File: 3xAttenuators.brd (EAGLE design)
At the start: 19 x 109.5 mm, 9 parts

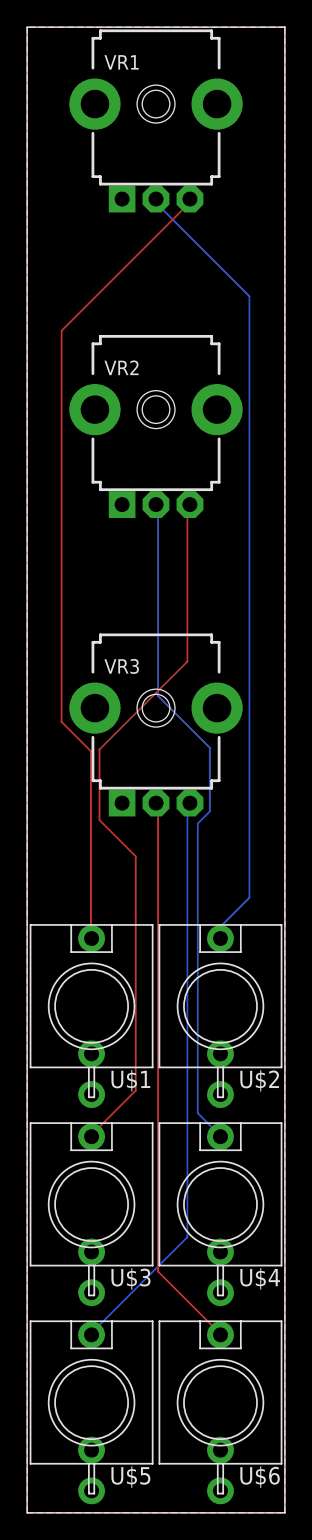
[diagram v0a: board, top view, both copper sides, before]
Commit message: adding rendered images of pcbs
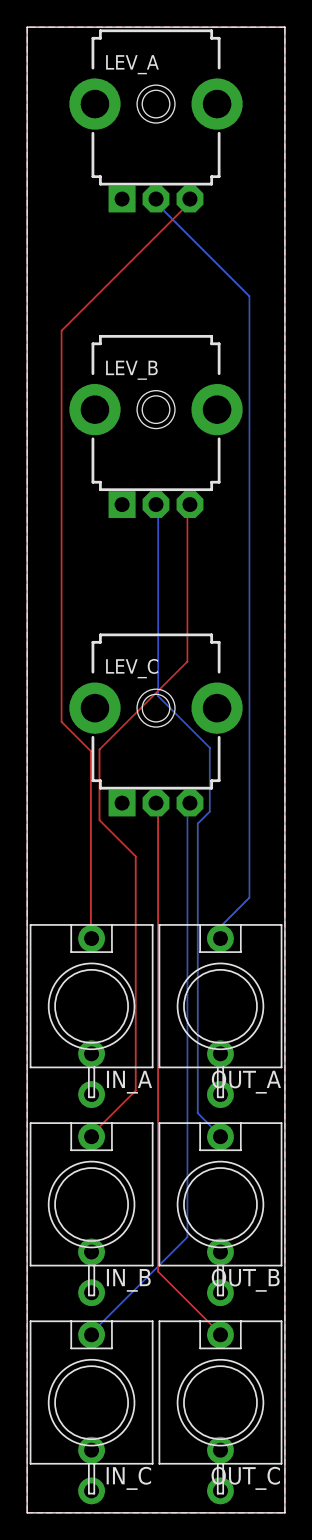
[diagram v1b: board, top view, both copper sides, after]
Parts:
- renumbered U$1 to IN_A, U$2 to OUT_A, U$3 to IN_B, U$4 to OUT_B, U$5 to IN_C, U$6 to OUT_C, VR1 to LEV_A, VR2 to LEV_B, VR3 to LEV_C
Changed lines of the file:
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@@
 </layers>
 <board>
+<fusionsync huburn="a.YnVzaW5lc3M6bXl1dzIwNDI" projecturn="a.YnVzaW5lc3M6bXl1dzIwNDIjRDIwMjIwNzA2NTM3OTQ1NzI2" f3durn="urn:adsk.wipprod:dm.lineage:7zFyWXWUTs2JKTcB2DoE3w" pcbguid="0d0611a9-9bd2-43dd-86c0-04be61c52497" lastpulledtime="" lastsyncedchangeguid="" latestrevisionid="42cfb351-0af1-4083-9baa-e86a03af3349" lastsyncedrevisionid="42cfb351-0af1-4083-9baa-e86a03af3349" lastboardhashguid="bff14a14-c0db-dd21-dd38-d28ebede1a6b" lastpushedtime="2022-12-21T20:23:48Z" linktopcb3d="true"/>
 <plain>
 <wire x1="0" y1="0" x2="19" y2="0" width="0" layer="20"/>
@@
 </autorouter>
 <elements>
-<element name="U$1" library="ES-2144 LPF Module" library_urn="urn:adsk.eagle:library:35649419" package="THONKICONN_WQP-PJ301M-12_JACK" package3d_urn="urn:adsk.eagle:package:35649430/2" value="THONKICONN_WQP-PJ301M-12_JACK" x="4.75" y="37.33" smashed="yes">
+<element name="IN_A" library="ES-2144 LPF Module" library_urn="urn:adsk.eagle:library:35649419" package="THONKICONN_WQP-PJ301M-12_JACK" package3d_urn="urn:adsk.eagle:package:35649430/2" value="THONKICONN_WQP-PJ301M-12_JACK" x="4.75" y="37.33" smashed="yes">
 <attribute name="NAME" x="9.2204" y="32.5802" size="1.27" layer="21" rot="R180"/>
 </element>
-<element name="U$2" library="ES-2144 LPF Module" library_urn="urn:adsk.eagle:library:35649419" package="THONKICONN_WQP-PJ301M-12_JACK" package3d_urn="urn:adsk.eagle:package:35649430/2" value="THONKICONN_WQP-PJ301M-12_JACK" x="14.25" y="37.33" smashed="yes">
+<element name="OUT_A" library="ES-2144 LPF Module" library_urn="urn:adsk.eagle:library:35649419" package="THONKICONN_WQP-PJ301M-12_JACK" package3d_urn="urn:adsk.eagle:package:35649430/2" value="THONKICONN_WQP-PJ301M-12_JACK" x="14.25" y="37.33" smashed="yes">
 <attribute name="NAME" x="18.7204" y="32.5802" size="1.27" layer="21" rot="R180"/>
 </element>
-<element name="U$3" library="ES-2144 LPF Module" library_urn="urn:adsk.eagle:library:35649419" package="THONKICONN_WQP-PJ301M-12_JACK" package3d_urn="urn:adsk.eagle:package:35649430/2" value="THONKICONN_WQP-PJ301M-12_JACK" x="4.75" y="22.725" smashed="yes">
+<element name="IN_B" library="ES-2144 LPF Module" library_urn="urn:adsk.eagle:library:35649419" package="THONKICONN_WQP-PJ301M-12_JACK" package3d_urn="urn:adsk.eagle:package:35649430/2" value="THONKICONN_WQP-PJ301M-12_JACK" x="4.75" y="22.725" smashed="yes">
 <attribute name="NAME" x="9.2204" y="17.9752" size="1.27" layer="21" rot="R180"/>
 </element>
-<element name="U$4" library="ES-2144 LPF Module" library_urn="urn:adsk.eagle:library:35649419" package="THONKICONN_WQP-PJ301M-12_JACK" package3d_urn="urn:adsk.eagle:package:35649430/2" value="THONKICONN_WQP-PJ301M-12_JACK" x="14.25" y="22.725" smashed="yes">
+<element name="OUT_B" library="ES-2144 LPF Module" library_urn="urn:adsk.eagle:library:35649419" package="THONKICONN_WQP-PJ301M-12_JACK" package3d_urn="urn:adsk.eagle:package:35649430/2" value="THONKICONN_WQP-PJ301M-12_JACK" x="14.25" y="22.725" smashed="yes">
 <attribute name="NAME" x="18.7204" y="17.9752" size="1.27" layer="21" rot="R180"/>
 </element>
-<element name="VR1" library="ES-2144 LPF Module" library_urn="urn:adsk.eagle:library:35649419" package="MUSICTHINGMODULAR_9MM_SNAP-IN_POT" package3d_urn="urn:adsk.eagle:package:35649433/2" value="B50K" x="9.5" y="103.83" smashed="yes">
+<element name="LEV_A" library="ES-2144 LPF Module" library_urn="urn:adsk.eagle:library:35649419" package="MUSICTHINGMODULAR_9MM_SNAP-IN_POT" package3d_urn="urn:adsk.eagle:package:35649433/2" value="B50K" x="9.5" y="103.83" smashed="yes">
 <attribute name="NAME" x="5.69" y="106.37" size="1.0668" layer="25"/>
 <attribute name="VALUE" x="5.69" y="100.02" size="1.27" layer="27"/>
 </element>
-<element name="VR2" library="ES-2144 LPF Module" library_urn="urn:adsk.eagle:library:35649419" package="MUSICTHINGMODULAR_9MM_SNAP-IN_POT" package3d_urn="urn:adsk.eagle:package:35649433/2" value="B50K" x="9.5" y="81.31" smashed="yes">
+<element name="LEV_B" library="ES-2144 LPF Module" library_urn="urn:adsk.eagle:library:35649419" package="MUSICTHINGMODULAR_9MM_SNAP-IN_POT" package3d_urn="urn:adsk.eagle:package:35649433/2" value="B50K" x="9.5" y="81.31" smashed="yes">
 <attribute name="NAME" x="5.69" y="83.85" size="1.0668" layer="25"/>
 <attribute name="VALUE" x="5.69" y="77.5" size="1.27" layer="27"/>
 </element>
-<element name="U$5" library="ES-2144 LPF Module" library_urn="urn:adsk.eagle:library:35649419" package="THONKICONN_WQP-PJ301M-12_JACK" package3d_urn="urn:adsk.eagle:package:35649430/2" value="THONKICONN_WQP-PJ301M-12_JACK" x="4.75" y="8.12" smashed="yes">
+<element name="IN_C" library="ES-2144 LPF Module" library_urn="urn:adsk.eagle:library:35649419" package="THONKICONN_WQP-PJ301M-12_JACK" package3d_urn="urn:adsk.eagle:package:35649430/2" value="THONKICONN_WQP-PJ301M-12_JACK" x="4.75" y="8.12" smashed="yes">
 <attribute name="NAME" x="9.2204" y="3.3702" size="1.27" layer="21" rot="R180"/>
 </element>
-<element name="U$6" library="ES-2144 LPF Module" library_urn="urn:adsk.eagle:library:35649419" package="THONKICONN_WQP-PJ301M-12_JACK" package3d_urn="urn:adsk.eagle:package:35649430/2" value="THONKICONN_WQP-PJ301M-12_JACK" x="14.25" y="8.12" smashed="yes">
+<element name="OUT_C" library="ES-2144 LPF Module" library_urn="urn:adsk.eagle:library:35649419" package="THONKICONN_WQP-PJ301M-12_JACK" package3d_urn="urn:adsk.eagle:package:35649430/2" value="THONKICONN_WQP-PJ301M-12_JACK" x="14.25" y="8.12" smashed="yes">
 <attribute name="NAME" x="18.7204" y="3.3702" size="1.27" layer="21" rot="R180"/>
 </element>
-<element name="VR3" library="ES-2144 LPF Module" library_urn="urn:adsk.eagle:library:35649419" package="MUSICTHINGMODULAR_9MM_SNAP-IN_POT" package3d_urn="urn:adsk.eagle:package:35649433/2" value="B50K" x="9.5" y="59.31" smashed="yes">
+<element name="LEV_C" library="ES-2144 LPF Module" library_urn="urn:adsk.eagle:library:35649419" package="MUSICTHINGMODULAR_9MM_SNAP-IN_POT" package3d_urn="urn:adsk.eagle:package:35649433/2" value="B50K" x="9.5" y="59.31" smashed="yes">
 <attribute name="NAME" x="5.69" y="61.85" size="1.0668" layer="25"/>
 <attribute name="VALUE" x="5.69" y="55.5" size="1.27" layer="27"/>
@@
 <signals>
 <signal name="N$3">
-<contactref element="U$3" pad="P$1"/>
-<contactref element="VR2" pad="3"/>
+<contactref element="IN_B" pad="P$1"/>
+<contactref element="LEV_B" pad="3"/>
 <wire x1="5.334" y1="28.321" x2="4.826" y2="27.813" width="0.127" layer="1"/>
 <wire x1="5.334" y1="28.448" x2="5.334" y2="28.321" width="0.127" layer="1"/>
@@
 </signal>
 <signal name="N$4">
-<contactref element="VR2" pad="2"/>
-<contactref element="U$4" pad="P$1"/>
+<contactref element="LEV_B" pad="2"/>
+<contactref element="OUT_B" pad="P$1"/>
 <wire x1="12.573" y1="29.464" x2="14.224" y2="27.813" width="0.127" layer="16"/>
 <wire x1="12.573" y1="50.8" x2="12.573" y2="29.464" width="0.127" layer="16"/>
@@
 </signal>
 <signal name="N$2">
-<contactref element="U$2" pad="P$1"/>
-<contactref element="VR1" pad="2"/>
+<contactref element="OUT_A" pad="P$1"/>
+<contactref element="LEV_A" pad="2"/>
 <wire x1="14.351" y1="43.307" x2="14.351" y2="42.418" width="0.127" layer="16"/>
 <wire x1="16.383" y1="45.339" x2="14.351" y2="43.307" width="0.127" layer="16"/>
@@
 </signal>
 <signal name="N$5">
-<contactref element="U$1" pad="P$1"/>
-<contactref element="VR1" pad="3"/>
+<contactref element="IN_A" pad="P$1"/>
+<contactref element="LEV_A" pad="3"/>
 <wire x1="4.699" y1="56.134" x2="4.699" y2="42.418" width="0.127" layer="1"/>
 <wire x1="2.54" y1="58.293" x2="4.699" y2="56.134" width="0.127" layer="1"/>
@@
 </signal>
 <signal name="N$1">
-<contactref element="U$5" pad="P$1"/>
-<contactref element="VR3" pad="3"/>
+<contactref element="IN_C" pad="P$1"/>
+<contactref element="LEV_C" pad="3"/>
 <wire x1="5.334" y1="13.716" x2="4.826" y2="13.208" width="0.127" layer="16"/>
 <wire x1="5.334" y1="13.843" x2="5.334" y2="13.716" width="0.127" layer="16"/>
@@
 </signal>
 <signal name="N$6">
-<contactref element="VR3" pad="2"/>
-<contactref element="U$6" pad="P$1"/>
+<contactref element="LEV_C" pad="2"/>
+<contactref element="OUT_C" pad="P$1"/>
 <wire x1="9.652" y1="17.78" x2="14.224" y2="13.208" width="0.127" layer="1"/>
 <wire x1="9.652" y1="52.07" x2="9.652" y2="17.78" width="0.127" layer="1"/>
@@
 <vertex x="19" y="0"/>
 </polygon>
-<contactref element="U$3" pad="P$3"/>
-<contactref element="VR2" pad="1"/>
-<contactref element="U$4" pad="P$3"/>
-<contactref element="U$1" pad="P$3"/>
-<contactref element="VR1" pad="1"/>
-<contactref element="U$2" pad="P$3"/>
-<contactref element="U$5" pad="P$3"/>
-<contactref element="VR3" pad="1"/>
-<contactref element="U$6" pad="P$3"/>
+<contactref element="IN_B" pad="P$3"/>
+<contactref element="LEV_B" pad="1"/>
+<contactref element="OUT_B" pad="P$3"/>
+<contactref element="IN_A" pad="P$3"/>
+<contactref element="LEV_A" pad="1"/>
+<contactref element="OUT_A" pad="P$3"/>
+<contactref element="IN_C" pad="P$3"/>
+<contactref element="LEV_C" pad="1"/>
+<contactref element="OUT_C" pad="P$3"/>
 <polygon width="0.1524" layer="16">
 <vertex x="19" y="109.5"/>
@@
 </note>
 <note version="8.3" severity="warning">
+Since Version 8.3, EAGLE supports Fusion synchronisation.
+This feature will not be available in this version and saving
+the document will break the link to the Fusion PCB feature.
+</note>
+<note version="8.3" severity="warning">
